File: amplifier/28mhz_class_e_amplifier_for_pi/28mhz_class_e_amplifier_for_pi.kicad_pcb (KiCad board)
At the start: 2 copper layers, 0 parts

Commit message: Everything except routing done
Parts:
- added C1: 10p, Capacitor_SMD:C_0805_2012Metric, F.Cu at (163.3, 96.5)
- added C2: 100pF, Capacitor_SMD:C_0603_1608Metric, F.Cu at (167.4, 97.3)
- added C3: 0.1u, Capacitor_SMD:C_0805_2012Metric, F.Cu at (129.1, 102.3)
- added C4: 0.33u, Capacitor_SMD:C_0805_2012Metric, F.Cu at (135.5, 102.3)
- added CF1: 120p, Capacitor_SMD:C_0805_2012Metric, F.Cu at (131.1, 72.1)
- added CF2: 220p, Capacitor_SMD:C_0805_2012Metric, F.Cu at (151.5, 72.0)
- added CF3: 120p, Capacitor_SMD:C_0805_2012Metric, F.Cu at (163.5, 72.0)
- added CL1: 110p, Capacitor_SMD:C_0805_2012Metric, F.Cu at (131.1, 78.2)
- added CS1: 200p, Capacitor_SMD:C_0805_2012Metric, F.Cu at (146.1, 79.0)
- added J1: Conn_Coaxial_Small, BNC:CONBNC002, F.Cu at (172.0, 70.5)
- added J2: 694106301002, barreljack:694106301002_1, F.Cu at (106.7, 89.3)
- added J3: Conn_01x03_Socket, Connector_PinSocket_2.54mm:PinSocket_1x03_P2.54mm_Vertical, F.Cu at (108.3, 100.2)
- added L1: 10µH, 10uH:B82144B__6.5D_, F.Cu at (145.2, 85.4)
- added L2_a1: 1.5µ, Inductor_SMD:L_0805_2012Metric, F.Cu at (162.1, 79.0)
- added L2_b1: 500n, wireinductor1:2929SQ501GEC, F.Cu at (160.8, 88.3)
- added LF1: 390n, wireinductor0:2929SQ391GEC, F.Cu at (132.5, 62.5)
- added LF2: 390n, wireinductor0:2929SQ391GEC, F.Cu at (157.5, 62.5)
- added LI1: 130n, custom:130nH_WLQC2222H0GR13LB, F.Cu at (138.4, 76.0)
- added M1: RD16HHF1, Package_TO_SOT_THT:TO-220-3_Vertical, B.Cu at (153.0, 96.4)
- added R0: 0, Resistor_SMD:R_2512_6332Metric, F.Cu at (143.4, 96.3)
- added R1: 0, Resistor_SMD:R_2512_6332Metric, F.Cu at (154.3, 79.0)
- added R2: 0, Resistor_SMD:R_2512_6332Metric, F.Cu at (126.7, 74.2)
- added RF1: 3.3k, Resistor_SMD:R_1206_3216Metric_Pad1.30x1.75mm_HandSolder, F.Cu at (137.1, 89.5)
- added RI1: 1k, Resistor_SMD:R_1206_3216Metric_Pad1.30x1.75mm_HandSolder, F.Cu at (129.5, 82.8)
- added U1: LT1818, LT1818:SOIC127P599X175-8N, F.Cu at (129.7, 89.5)
- added U2: LM7805_TO220, Package_TO_SOT_THT:TO-220-3_Vertical, F.Cu at (134.2, 95.9)

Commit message: almost done, probably
check pinouts, op amp might be peculiar
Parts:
- C1, C3, C4, CF1, CF2, CF3, CL1, CS1: footprint Capacitor_SMD:C_0805_2012Metric -> Capacitor_SMD:C_0805_2012Metric_Pad1.18x1.45mm_HandSolder
- C2: footprint Capacitor_SMD:C_0603_1608Metric -> Capacitor_SMD:C_0603_1608Metric_Pad1.08x0.95mm_HandSolder
- L2_a1: footprint Inductor_SMD:L_0805_2012Metric -> Inductor_SMD:L_0805_2012Metric_Pad1.05x1.20mm_HandSolder
- R0, R1, R2: footprint Resistor_SMD:R_2512_6332Metric -> Resistor_SMD:R_2512_6332Metric_Pad1.40x3.35mm_HandSolder
- moved M1 1.91 mm to (151.1, 96.3)
- turned C2 to -90 degrees
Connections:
- C3 pad 2: GND -> 0
- C4 pad 2: GND -> 0
- J2 pad 2: GND -> 0
- J2 pad 3: GND -> 0
- J3 pad 3: GND -> 0
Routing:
- net 0: track 0.00 -> 134.4 mm, vias 0 -> 9
- net Net-(J2-POWER): track 0.00 -> 32.7 mm
- net Net-(J3-Pin_1): track 0.00 -> 27.6 mm
- net Net-(J3-Pin_2): track 0.00 -> 26.6 mm
- net Net-(M1-D): track 0.00 -> 26.5 mm
- net Net-(CF2-Pad1): track 0.00 -> 22.1 mm
- net Net-(C2-Pad1): track 0.00 -> 19.4 mm
- net Net-(J1-In): track 0.00 -> 17.3 mm
- net Net-(U1-OUT): track 0.00 -> 14.9 mm
- net Net-(L2_a1-Pad1): track 0.00 -> 14.3 mm
- net Net-(CL1-Pad2): track 0.00 -> 14.2 mm
- net Net-(U1-IN-): track 0.00 -> 13.2 mm
- net Net-(CF1-Pad1): track 0.00 -> 13.1 mm
- net Net-(U2-VI): track 0.00 -> 7.38 mm
- net Net-(M1-G): track 0.00 -> 4.70 mm
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- added copper zone on B.Cu, net 0
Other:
- board outline added: 92.2 x 49.2 mm

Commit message: more design
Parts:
- M1: moved to F.Cu
- moved RF1 8.89 mm to (129.6, 94.3), turned to 180 degrees
- moved C2 4.10 mm to (167.4, 101.5)
- moved R0 4.10 mm to (143.4, 100.5)
- moved C1 4.10 mm to (163.3, 100.5)
- moved M1 4.10 mm to (151.1, 100.4)
- moved U2 1.75 mm to (134.2, 97.7)
- moved CL1 0.40 mm to (131.1, 77.8)
- turned U1 to 0 degrees
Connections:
- C4 pad 1: Net-(U2-VI) -> Net-(J2-POWER)
- U1 pad 1: Net-(J3-Pin_2) -> (no net)
- U1 pad 3: Net-(U1-OUT) -> Net-(J3-Pin_2)
- U1 pad 4: Net-(J2-POWER) -> 0
- U1 pad 5: 0 -> (no net)
- U1 pad 6: (no net) -> Net-(U1-OUT)
- U1 pad 7: (no net) -> Net-(J2-POWER)
- U2 pad 1: Net-(U2-VI) -> Net-(J2-POWER)
- U2 pad 2: GND -> 0
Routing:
- net 0: track 134.4 -> 2.66 mm
- net Net-(J2-POWER): track 32.7 -> 53.7 mm
- net Net-(U2-VI): track 7.38 -> 0.00 mm
- net Net-(J3-Pin_2): track 26.6 -> 21.7 mm
- net Net-(C2-Pad1): track 19.4 -> 24.0 mm
- net Net-(U1-OUT): track 14.9 -> 19.2 mm
- net Net-(M1-S): track 26.5 -> 30.6 mm
- net Net-(J3-Pin_1): track 27.6 -> 24.6 mm
- net Net-(CL1-Pad1): track 4.43 -> 5.35 mm
- net Net-(J1-In): track 17.3 -> 18.2 mm
- net Net-(U1-IN-): track 13.2 -> 13.8 mm

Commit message: fix transistor pinout, probably sleep soon
this is hard and i don't want to frick up since shipping is really expensive
TODO check preamp, then check over entire circuit, then order PCBs (JLCPCB), components (Mouser), power hardware (Amazon?), BNC cable (Amazon?), antenna, soldering iron (Pinecil?), uhhhhh why is getting into radio so expensive
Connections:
- C1 pad 1: Net-(M1-S) -> Net-(M1-D)
- C2 pad 2: Net-(M1-S) -> Net-(M1-D)
- L1 pad 2: Net-(M1-S) -> Net-(M1-D)
- M1 pad 1: Net-(M1-S) -> 0
- M1 pad 3: 0 -> Net-(M1-D)
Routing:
- net Net-(M1-S): track 30.6 -> 0.00 mm
- net Net-(M1-D): track 0.00 -> 28.8 mm
- net 0: vias 9 -> 24
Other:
- board size 92.2 x 49.2 mm -> 81.5 x 49.2 mm
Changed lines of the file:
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@@
 		(0 "F.Cu" signal)
 		(31 "B.Cu" signal)
-		(32 "B.Adhes" user "B.Adhesive")
-		(33 "F.Adhes" user "F.Adhesive")
-		(34 "B.Paste" user)
-		(35 "F.Paste" user)
 		(36 "B.SilkS" user "B.Silkscreen")
 		(37 "F.SilkS" user "F.Silkscreen")
 		(38 "B.Mask" user)
 		(39 "F.Mask" user)
-		(40 "Dwgs.User" user "User.Drawings")
-		(41 "Cmts.User" user "User.Comments")
-		(42 "Eco1.User" user "User.Eco1")
-		(43 "Eco2.User" user "User.Eco2")
 		(44 "Edge.Cuts" user)
 		(45 "Margin" user)
 		(46 "B.CrtYd" user "B.Courtyard")
 		(47 "F.CrtYd" user "F.Courtyard")
-		(48 "B.Fab" user)
-		(49 "F.Fab" user)
-		(50 "User.1" user)
-		(51 "User.2" user)
-		(52 "User.3" user)
-		(53 "User.4" user)
-		(54 "User.5" user)
-		(55 "User.6" user)
-		(56 "User.7" user)
-		(57 "User.8" user)
-		(58 "User.9" user)
 	)
 	(setup
@@
 		(allow_soldermask_bridges_in_footprints no)
 		(pcbplotparams
-			(layerselection 0x00010fc_ffffffff)
+			(layerselection 0x00010f0_ffffffff)
 			(plot_on_all_layers_selection 0x0000000_00000000)
 			(disableapertmacros no)
-			(usegerberextensions no)
+			(usegerberextensions yes)
 			(usegerberattributes yes)
 			(usegerberadvancedattributes yes)
@@
 			(plotinvisibletext no)
 			(sketchpadsonfab no)
-			(subtractmaskfromsilk no)
+			(subtractmaskfromsilk yes)
 			(outputformat 1)
 			(mirror no)
-			(drillshape 1)
+			(drillshape 0)
 			(scaleselection 1)
-			(outputdirectory "")
+			(outputdirectory "plots/")
 		)
 	)
@@
 	(net 14 "Net-(L2_a1-Pad1)")
 	(net 15 "Net-(M1-G)")
-	(net 16 "Net-(M1-S)")
+	(net 16 "Net-(M1-D)")
 	(footprint "Resistor_SMD:R_2512_6332Metric_Pad1.40x3.35mm_HandSolder"
 		(layer "F.Cu")
@@
 			(layers "F.Cu" "F.Paste" "F.Mask")
 			(roundrect_rratio 0.212766)
-			(net 16 "Net-(M1-S)")
+			(net 16 "Net-(M1-D)")
 			(pintype "passive")
 		)
@@
 		(tags "TO-220-3 Vertical RM 2.54mm")
 		(property "Reference" "M1"
-			(at 2.54 -4.27 360)
+			(at 2.54 -4.27 0)
 			(layer "F.SilkS")
 			(effects
@@
 		)
 		(property "Value" "RD16HHF1"
-			(at 2.54 2.5 360)
+			(at 2.54 2.5 0)
 			(layer "F.Fab")
 			(effects
@@
 		)
 		(fp_text user "${REFERENCE}"
-			(at 2.54 -4.27 360)
+			(at 2.54 -4.27 0)
 			(layer "F.Fab")
 			(effects
@@
 			(layers "*.Cu" "*.Mask")
 			(remove_unused_layers no)
-			(net 16 "Net-(M1-S)")
+			(net 1 "0")
 			(pinfunction "D")
 			(pintype "passive")
@@
 			(layers "*.Cu" "*.Mask")
 			(remove_unused_layers no)
-			(net 1 "0")
+			(net 16 "Net-(M1-D)")
 			(pinfunction "S")
 			(pintype "passive")
@@
 		(tags "Integrated Circuit")
 		(property "Reference" "U1"
-			(at 0 0 360)
+			(at 0 0 0)
 			(layer "F.SilkS")
 			(effects
@@
 		)
 		(property "Value" "LT1818"
-			(at 0 0 360)
+			(at 0 0 0)
 			(layer "F.SilkS")
 			(hide yes)
@@
 		)
 		(property "Footprint" "LT1818:SOIC127P599X175-8N"
-			(at 0 0 360)
+			(at 0 0 0)
 			(layer "F.Fab")
 			(hide yes)
@@
 		)
 		(property "Datasheet" ""
-			(at 0 0 360)
+			(at 0 0 0)
 			(layer "F.Fab")
 			(hide yes)
@@
 		)
 		(property "Description" ""
-			(at 0 0 360)
+			(at 0 0 0)
 			(layer "F.Fab")
 			(hide yes)
@@
 		)
 		(fp_text user "${REFERENCE}"
-			(at 0 0 360)
+			(at 0 0 0)
 			(layer "F.Fab")
 			(effects
@@
 			(layers "F.Cu" "F.Paste" "F.Mask")
 			(roundrect_rratio 0.25)
-			(net 16 "Net-(M1-S)")
+			(net 16 "Net-(M1-D)")
 			(pintype "passive")
 		)
@@
 			(layers "*.Cu" "*.Mask")
 			(remove_unused_layers no)
-			(net 16 "Net-(M1-S)")
+			(net 16 "Net-(M1-D)")
 			(pintype "passive")
 		)
@@
 		(tags "resistor handsolder")
 		(property "Reference" "RF1"
-			(at 0 -1.82 360)
+			(at 0 -1.82 0)
 			(layer "F.SilkS")
 			(effects
@@
 		)
 		(property "Value" "3.3k"
-			(at 0 1.82 360)
+			(at 0 1.82 0)
 			(layer "F.Fab")
 			(effects
@@
 		)
 		(fp_text user "${REFERENCE}"
-			(at 0 0 360)
+			(at 0 0 0)
 			(layer "F.Fab")
 			(effects
@@
 	(gr_rect
 		(start 104.925 55.8)
-		(end 180.525 104.975)
-		(stroke
-			(width 0.2)
-			(type default)
-		)
-		(fill none)
-		(layer "F.Cu")
-	)
-	(gr_rect
-		(start 104.925 55.8)
-		(end 197.1 104.95)
+		(end 186.375 104.95)
 		(stroke
 			(width 0.05)
@@
 	)
 	(via
-		(at 163.5 72.975)
+		(at 138.45 72.875)
+		(size 1.5)
+		(drill 1)
+		(layers "F.Cu" "B.Cu")
+		(net 1)
+	)
+	(via
+		(at 130.65 72.875)
 		(size 0.6)
 		(drill 0.3)
@@
 	)
 	(via
-		(at 138.45 72.875)
+		(at 163.5 73.25)
+		(size 0.6)
+		(drill 0.3)
+		(layers "F.Cu" "B.Cu")
+		(net 1)
+	)
+	(via
+		(at 127.7 83.25)
+		(size 0.6)
+		(drill 0.3)
+		(layers "F.Cu" "B.Cu")
+		(net 1)
+	)
+	(via
+		(at 131.05 73.4)
+		(size 0.6)
+		(drill 0.3)
+		(layers "F.Cu" "B.Cu")
+		(net 1)
+	)
+	(via
+		(at 129.9 101.95)
+		(size 0.6)
+		(drill 0.3)
+		(layers "F.Cu" "B.Cu")
+		(net 1)
+	)
+	(via
+		(at 163.1 72.725)
+		(size 0.6)
+		(drill 0.3)
+		(layers "F.Cu" "B.Cu")
+		(net 1)
+	)
+	(via
+		(at 128.225 82.85)
+		(size 0.6)
+		(drill 0.3)
+		(layers "F.Cu" "B.Cu")
+		(net 1)
+	)
+	(via
+		(at 162 100.15)
 		(size 0.6)
 		(drill 0.3)
@@
 	)
 	(via
-		(at 134.5 102.35)
+		(at 131.45 72.875)
 		(size 0.6)
 		(drill 0.3)
@@
 	)
 	(via
-		(at 162.275 100.55)
+		(at 151.5 73.3)
 		(size 0.6)
 		(drill 0.3)
@@
 	)
 	(via
-		(at 151.5 73.05)
+		(at 134.75 102.35)
 		(size 0.6)
 		(drill 0.3)
@@
 	)
 	(via
-		(at 127.95 82.85)
+		(at 151.9 72.775)
 		(size 0.6)
 		(drill 0.3)
@@
 	)
 	(via
-		(at 126.925 91.35)
+		(at 151.1 72.775)
 		(size 0.6)
 		(drill 0.3)
@@
 	)
 	(via
-		(at 131.05 73.15)
+		(at 126.5 91.35)
 		(size 0.6)
 		(drill 0.3)
@@
 	)
 	(via
-		(at 130.175 102.35)
+		(at 130.425 102.35)
+		(size 0.6)
+		(drill 0.3)
+		(layers "F.Cu" "B.Cu")
+		(net 1)
+	)
+	(via
+		(at 134.225 102.75)
+		(size 0.6)
+		(drill 0.3)
+		(layers "F.Cu" "B.Cu")
+		(net 1)
+	)
+	(via
+		(at 163.9 72.725)
+		(size 0.6)
+		(drill 0.3)
+		(layers "F.Cu" "B.Cu")
+		(net 1)
+	)
+	(via
+		(at 134.225 101.95)
+		(size 0.6)
+		(drill 0.3)
+		(layers "F.Cu" "B.Cu")
+		(net 1)
+	)
+	(via
+		(at 162 100.95)
+		(size 0.6)
+		(drill 0.3)
+		(layers "F.Cu" "B.Cu")
+		(net 1)
+	)
+	(via
+		(at 127.7 82.45)
+		(size 0.6)
+		(drill 0.3)
+		(layers "F.Cu" "B.Cu")
+		(net 1)
+	)
+	(via
+		(at 162.525 100.55)
+		(size 0.6)
+		(drill 0.3)
+		(layers "F.Cu" "B.Cu")
+		(net 1)
+	)
+	(via
+		(at 129.9 102.75)
+		(size 0.6)
+		(drill 0.3)
+		(layers "F.Cu" "B.Cu")
+		(net 1)
+	)
+	(via
+		(at 127.375 91.35)
 		(size 0.6)
 		(drill 0.3)
@@
 	)
 	(segment
-		(start 153.64 99.41)
-		(end 153.64 100.425)
+		(start 146.2275 90.425)
+		(end 145.2 90.425)
 		(width 1.25)
 		(layer "F.Cu")
@@
 	)
 	(segment
-		(start 153.64 100.425)
-		(end 153.64 98.865)
+		(start 156.18 100.3775)
+		(end 146.2275 90.425)
 		(width 1.25)
 		(layer "F.Cu")
@@
 	)
 	(segment
-		(start 166.1 102.3125)
-		(end 164.3375 100.55)
+		(start 157.605 99)
+		(end 156.18 100.425)
 		(width 1.25)
 		(layer "F.Cu")
@@
 	)
 	(segment
-		(start 164.3375 100.55)
-		(end 164.3375 99.825)
+		(start 163.5125 99)
+		(end 157.605 99)
 		(width 1.25)
 		(layer "F.Cu")
@@
 	)
 	(segment
-		(start 164.3375 99.825)
-		(end 163.1125 98.6)
+		(start 163.5125 99)
+		(end 164.3375 99.825)
 		(width 1.25)
 		(layer "F.Cu")
@@
 	)
 	(segment
-		(start 163.1125 98.6)
-		(end 154.45 98.6)
+		(start 164.3375 99.825)
+		(end 164.3375 100.55)
 		(width 1.25)
 		(layer "F.Cu")
@@
 	)
 	(segment
-		(start 166.1 102.3125)
-		(end 167.4 102.3125)
+		(start 164.3375 100.55)
+		(end 166.1 102.3125)
 		(width 1.25)
 		(layer "F.Cu")
@@
 	)
 	(segment
-		(start 153.64 98.865)
-		(end 145.2 90.425)
+		(start 166.1 102.3125)
+		(end 167.4 102.3125)
 		(width 1.25)
 		(layer "F.Cu")
@@
 	)
 	(segment
-		(start 154.45 98.6)
-		(end 153.64 99.41)
+		(start 156.18 100.425)
+		(end 156.18 100.3775)
 		(width 1.25)
 		(layer "F.Cu")
@@
 		(polygon
 			(pts
-				(xy 106.025 103.95) (xy 180 103.95) (xy 180 65.25) (xy 179.825 65.075) (xy 106.025 65.075)
+				(xy 106.025 103.95) (xy 185.4 103.95) (xy 185.4 56.975) (xy 106.025 56.975)
 			)
 		)

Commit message: fancy text(TM)
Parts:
- renumbered U2 to LM7805, M1 to RD16HHF1
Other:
- board text added: "10m Class E amplifier"
- board text added: "12V input"
- board text added: "5V"
- board text added: "BNC output"
- board text added: "D"
- board text added: "G"
- board text added: "GND"
- board text added: "HiPi"
- board text added: "I"
- board text added: "KQ4TVW Ben Goldberg"
- board text added: "O"
- board text added: "RF"
- board text added: "S"
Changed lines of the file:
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@@
 		(descr "TO-220-3, Vertical, RM 2.54mm, see https://www.vishay.com/docs/66542/to-220-1.pdf")
 		(tags "TO-220-3 Vertical RM 2.54mm")
-		(property "Reference" "M1"
+		(property "Reference" "RD16HHF1"
 			(at 2.54 -4.27 0)
 			(layer "F.SilkS")
@@
 		(tags "capacitor handsolder")
 		(property "Reference" "C3"
-			(at 0 -1.68 0)
+			(at -3.175 0 0)
 			(layer "F.SilkS")
 			(effects
@@
 		(descr "TO-220-3, Vertical, RM 2.54mm, see https://www.vishay.com/docs/66542/to-220-1.pdf")
 		(tags "TO-220-3 Vertical RM 2.54mm")
-		(property "Reference" "U2"
-			(at 2.54 -4.27 0)
+		(property "Reference" "LM7805"
+			(at 10.915 -0.02 0)
 			(layer "F.SilkS")
 			(effects
@@
 		(tags "resistor handsolder")
 		(property "Reference" "RF1"
-			(at 0 -1.82 0)
+			(at 4.175 0 0)
 			(layer "F.SilkS")
 			(effects
@@
 		(layer "Edge.Cuts")
 	)
+	(gr_text "GND"
+		(at 110.35 95.7 0)
+		(layer "F.SilkS")
+		(effects
+			(font
+				(size 1 1)
+				(thickness 0.2)
+				(bold yes)
+			)
+			(justify left bottom)
+		)
+	)
+	(gr_text "S"
+		(at 153.125 98.55 0)
+		(layer "F.SilkS")
+		(effects
+			(font
+				(size 1 1)
+				(thickness 0.1)
+			)
+			(justify left bottom)
+		)
+	)
+	(gr_text "10m Class E amplifier"
+		(at 106.8 65.55 0)
+		(layer "F.SilkS")
+		(effects
+			(font
+				(size 1 1)
+				(thickness 0.1)
+			)
+			(justify left bottom)
+		)
+	)
+	(gr_text "O"
+		(at 127.625 100.8 0)
+		(layer "F.SilkS")
+		(effects
+			(font
+				(size 1 1)
+				(thickness 0.1)
+			)
+			(justify left bottom)
+		)
+	)
+	(gr_text "HiPi"
+		(at 105.8 63.675 0)
+		(layer "F.SilkS")
+		(effects
+			(font
+				(size 5 5)
+				(thickness 0.2)
+			)
+			(justify left bottom)
+		)
+	)
+	(gr_text "KQ4TVW\nBen Goldberg"
+		(at 184.125 102.275 0)
+		(layer "F.SilkS")
+		(effects
+			(font
+				(size 1.18 1.18)
+				(thickness 0.25)
+				(bold yes)
+			)
+			(justify right bottom)
+		)
+	)
+	(gr_text "12V input"
+		(at 106.7095 79.825 0)
+		(layer "F.SilkS")
+		(effects
+			(font
+				(size 1 1)
+				(thickness 0.2)
+				(bold yes)
+			)
+			(justify left bottom)
+		)
+	)
+	(gr_text "BNC output"
+		(at 171.5 61.85 0)
+		(layer "F.SilkS")
+		(effects
+			(font
+				(size 1.5 1.5)
+				(thickness 0.2)
+				(bold yes)
+			)
+			(justify left bottom)
+		)
+	)
+	(gr_text "RF"
+		(at 110.35 98.2 0)
+		(layer "F.SilkS")
+		(effects
+			(font
+				(size 1 1)
+				(thickness 0.2)
+				(bold yes)
+			)
+			(justify left bottom)
+		)
+	)
+	(gr_text "5V"
+		(at 110.35 100.7 0)
+		(layer "F.SilkS")
+		(effects
+			(font
+				(size 1 1)
+				(thickness 0.2)
+				(bold yes)
+			)
+			(justify left bottom)
+		)
+	)
+	(gr_text "I"
+		(at 134.925 100.8 0)
+		(layer "F.SilkS")
+		(effects
+			(font
+				(size 1 1)
+				(thickness 0.1)
+			)
+			(justify left bottom)
+		)
+	)
+	(gr_text "G"
+		(at 149.6 98.55 0)
+		(layer "F.SilkS")
+		(effects
+			(font
+				(size 1 1)
+				(thickness 0.1)
+			)
+			(justify left bottom)
+		)
+	)
+	(gr_text "D\n"
+		(at 156.625 98.55 0)
+		(layer "F.SilkS")
+		(effects
+			(font
+				(size 1 1)
+				(thickness 0.1)
+			)
+			(justify left bottom)
+		)
+	)
+	(gr_text "G"
+		(at 131.15 100.8 0)
+		(layer "F.SilkS")
+		(effects
+			(font
+				(size 1 1)
+				(thickness 0.1)
+			)
+			(justify left bottom)
+		)
+	)
 	(segment

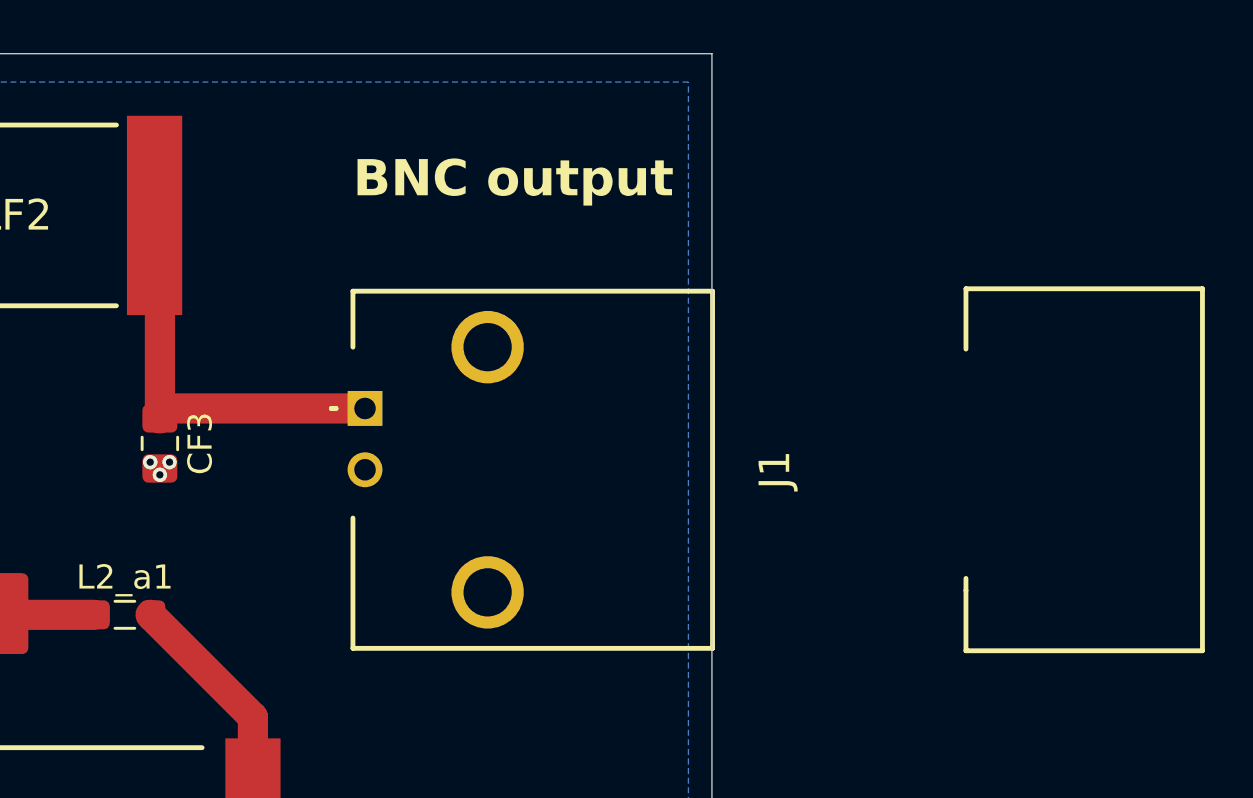
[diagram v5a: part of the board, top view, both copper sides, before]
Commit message: ready for ordering!
just fixed BNC polarity and untented vias
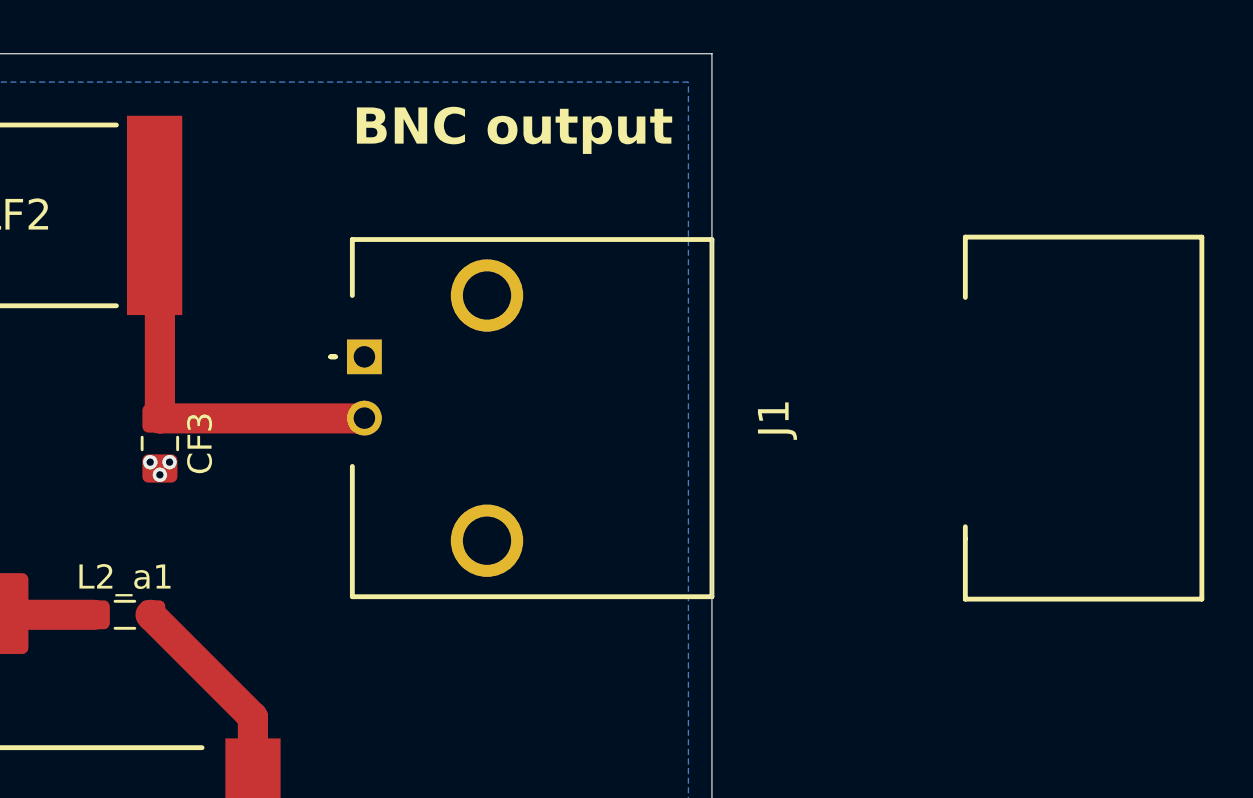
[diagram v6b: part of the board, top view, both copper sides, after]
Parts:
- moved J1 2.14 mm to (172.0, 68.4)
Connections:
- J1 pad 1: Net-(J1-In) -> 0
- J1 pad 2: 0 -> Net-(J1-In)
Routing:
- net Net-(J1-In): track 18.2 -> 18.9 mm
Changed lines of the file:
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@@
 	(footprint "BNC:CONBNC002"
 		(layer "F.Cu")
-		(at 172 70.5 -90)
+		(at 171.975 68.36 -90)
 		(descr "CONBNC002-3")
 		(tags "Connector")
@@
 			(layers "*.Cu" "*.Mask")
 			(remove_unused_layers no)
-			(net 9 "Net-(J1-In)")
+			(net 1 "0")
 			(pinfunction "In")
 			(pintype "passive")
@@
 			(layers "*.Cu" "*.Mask")
 			(remove_unused_layers no)
-			(net 1 "0")
+			(net 9 "Net-(J1-In)")
 			(pinfunction "Ext")
 			(pintype "passive")
@@
 	)
 	(gr_text "BNC output"
-		(at 171.5 61.85 0)
+		(at 171.475 59.71 0)
 		(layer "F.SilkS")
 		(effects
@@
 	)
 	(segment
-		(start 163.5 62.72)
-		(end 163.28 62.5)
+		(start 171.9625 70.9125)
+		(end 171.975 70.9)
 		(width 0.2)
 		(layer "F.Cu")
@@
 	)
 	(segment
-		(start 163.28 70.78)
-		(end 163.5 71)
+		(start 163.9125 70.5)
+		(end 163.5 70.9125)
 		(width 0.2)
 		(layer "F.Cu")
@@
 	)
 	(segment
-		(start 163.9125 70.5)
-		(end 163.5 70.9125)
+		(start 163.5 62.72)
+		(end 163.28 62.5)
+		(width 0.2)
+		(layer "F.Cu")
+		(net 9)
+	)
+	(segment
+		(start 163.28 70.78)
+		(end 163.5 71)
 		(width 0.2)
 		(layer "F.Cu")
@@
 	)
 	(segment
-		(start 172 70.5)
-		(end 163.9125 70.5)
+		(start 171.7625 70.9125)
+		(end 171.975 70.7)
+		(width 0.2)
+		(layer "F.Cu")
+		(net 9)
+	)
+	(segment
+		(start 163.5 70.9125)
+		(end 171.9625 70.9125)
 		(width 1.25)
 		(layer "F.Cu")
